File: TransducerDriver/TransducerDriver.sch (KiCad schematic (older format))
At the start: 18 parts, among them Q3 IRF540N, Q4 IRF540N, T2 Transformer_SP_1S 1:10

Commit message: studies on transducer
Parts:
- removed C?: 159nF, symbol Device:C
- removed C?: 10nF, symbol Device:C
- removed R? (x2): 4K, symbol Device:R
- removed R?: 2Khom, symbol Device:R
- removed R?: 1Kohm, symbol Device:R
- removed R? (x2): 101, symbol Device:R
- removed Rshut3: 0.01, Resistors_THT:R_Axial_DIN0207_L6.3mm_D2.5mm_P10.16mm_Horizontal, symbol Device:R
- removed Rtrans2: 10K, Resistors_THT:R_Axial_DIN0207_L6.3mm_D2.5mm_P10.16mm_Horizontal, symbol Device:R
- removed U? (x2): INA217, symbol Amplifier_Instrumentation:INA217
- added C2In1, C2In2, C2out1, C3, C4, Cgnd2, Cref2: 0.1u, Capacitors_THT:C_Disc_D5.0mm_W2.5mm_P5.00mm, symbol Device:C_Small
- added Cadc1: 10pf, Capacitors_THT:C_Disc_D8.0mm_W5.0mm_P7.50mm, symbol Device:C
- added Cb1: 10nF, Capacitors_THT:C_Disc_D5.0mm_W2.5mm_P5.00mm, symbol Device:C_Small
- added Cb?: 0.1uF, Capacitors_THT:C_Disc_D5.0mm_W2.5mm_P5.00mm, symbol Device:C_Small
- added Cenv1: 10nf, Capacitors_THT:C_Disc_D5.0mm_W2.5mm_P5.00mm, symbol Device:C_Small
- added Cg1: 0.47uF, Capacitors_THT:C_Disc_D5.0mm_W2.5mm_P5.00mm, symbol Device:C_Small
- added D2: 1N4007, Diodes_THT:D_DO-35_SOD27_P10.16mm_Horizontal, symbol Device:D
- added Dz1, Dz2, Dz3: 3.3V, symbol Device:D_Zener
- added J1: ModSigJack, symbol Connector:Conn_01x02_Female
- added J2: BattJack+, symbol Connector:Conn_01x01_Male
- added J3: BattJack-, symbol Connector:Conn_01x01_Male
- added Jadc1: connADC, symbol Connector:Conn_01x01_Male
- added R2: 1K, Resistors_THT:R_Axial_DIN0207_L6.3mm_D2.5mm_P10.16mm_Horizontal, symbol Device:R
- added R2F1: 100Kohm, Resistors_THT:R_Axial_DIN0309_L9.0mm_D3.2mm_P12.70mm_Horizontal, symbol Device:R
- added R2G1: 1Kohm, Resistors_THT:R_Axial_DIN0309_L9.0mm_D3.2mm_P12.70mm_Horizontal, symbol Device:R
- added Radc1: 2.5K, Resistors_THT:R_Axial_DIN0309_L9.0mm_D3.2mm_P12.70mm_Horizontal, symbol Device:R
- added Rb1, Rb2: 5K, Resistors_THT:R_Axial_DIN0309_L9.0mm_D3.2mm_P12.70mm_Horizontal, symbol Device:R
- added Rbias1, Rbias2: 2.2K, Resistors_THT:R_Axial_DIN0309_L9.0mm_D3.2mm_P12.70mm_Horizontal, symbol Device:R
- added Rbuf1: 10ohm, Resistors_THT:R_Axial_DIN0309_L9.0mm_D3.2mm_P12.70mm_Horizontal, symbol Device:R
- added Rf2, Rin2: 200K, Resistors_THT:R_Axial_DIN0309_L9.0mm_D3.2mm_P12.70mm_Horizontal, symbol Device:R
- added Rg1: 2K, Resistors_THT:R_Axial_DIN0309_L9.0mm_D3.2mm_P12.70mm_Horizontal, symbol Device:R
- added Rgain1: 101, Resistors_THT:R_Axial_DIN0309_L9.0mm_D3.2mm_P12.70mm_Horizontal, symbol Device:R
- added U1: TL082, symbol Amplifier_Operational:TL082
- added U2: INA217-Amplifier_Instrumentation, symbol TransducerDriver-rescue:INA217-Amplifier_Instrumentation
- added U3: TC427, Housings_DIP:DIP-8_W7.62mm_LongPads, symbol TransducerDriver-rescue:TC427-Driver_FET
- added U4: LM4562, symbol Amplifier_Operational:LM4562
- added Y2: Crystal, Wire_Connections_Bridges:WireConnection_2.50mmDrill, symbol Device:Crystal
- added Y3: FishFinder, Wire_Connections_Bridges:WireConnection_2.50mmDrill, symbol Device:Crystal
- D1: renamed from D?; footprint (none) -> Diodes_THT:D_5W_P12.70mm_Horizontal
- Q3, Q4: footprint Package_TO_SOT_THT:TO-220-3_Vertical -> TO_SOT_Packages_THT:TO-220-3_Vertical
- Renv1: renamed from R?; value 530 -> 2K; footprint (none) -> Resistors_THT:R_Axial_DIN0309_L9.0mm_D3.2mm_P12.70mm_Horizontal
- T1: renamed from T2; footprint Transformer_THT:Transformer_Toroid_Tapped_Horizontal_D10.5mm_Amidon-T37 -> Transformers_THT:Transformer_Toroid_Tapped_Horizontal_D14.0mm_Amidon-T50
- Y1: renamed from Y?; footprint (none) -> Wire_Connections_Bridges:WireConnection_2.50mmDrill
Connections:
- net labels added: ADCinput, ModSig+, ModSig-, Prob1, Prob2, Stage1Out, Stage2Out, Vin
- net labels removed: MicroInput, SigA, SigB, VCC
- wire segments 60 -> 125
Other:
- note added: "10Khz HP filter\n0.1uF 1Kohm"
- note added: "6Kohm Internal \nR. Is it High \noutput Impedance?"
- note added: "ADC internal"
- note added: "Envelope\nDetector"
- note added: "First Stage \nDiff Amp"
- note added: "Impedance Measure Circuit"
- note added: "Inverting \nSimple Vref"
- note added: "Measure"
- note added: "Non-Inverting\nHigh Impedance"
- note added: "Potential\nVariable \nGain"
- note added: "Rin2 same as R2 \nlimit input bias current"
- note added: "Transmitter"
- note added: "Two Options for second stage"
- note added: "Vref Gen"
- note added: "X cgnd1<<Rg2 \nF = 20Khz\nC = 0.47uF \nXc = 17ohm"
- note added: "bias current \nsupply\n0.1uF 2.2Kohm\nFc = 4.5Khz"
- note added: "half battery Vref generator \nwith small resistor Rbuf1\nprevernt opamp unstable"
- note added: "min Fcarr = 40Khz \nmax Fmod = 1Khz \n10nF 2Kohm\nFc = 8Kohm"
- note added: "sine wave input"
- note removed: "-3dB @ 30Khz"
- note removed: "40dB gain\n= 101ohm RG"
- note removed: "6K output impedence"
- note removed: "Driver"
- note removed: "Highpass Assuming \n1K impedance. \n1Khz cutoff feq"
- note removed: "Over Amplify \nthen voltage devide \nto reduce diode bias"
- note removed: "amplify signal at \nhalf battery voltage. \n(fake negative voltage)"
- moved on the sheet: D1, Q3, Renv1, T1, Y1

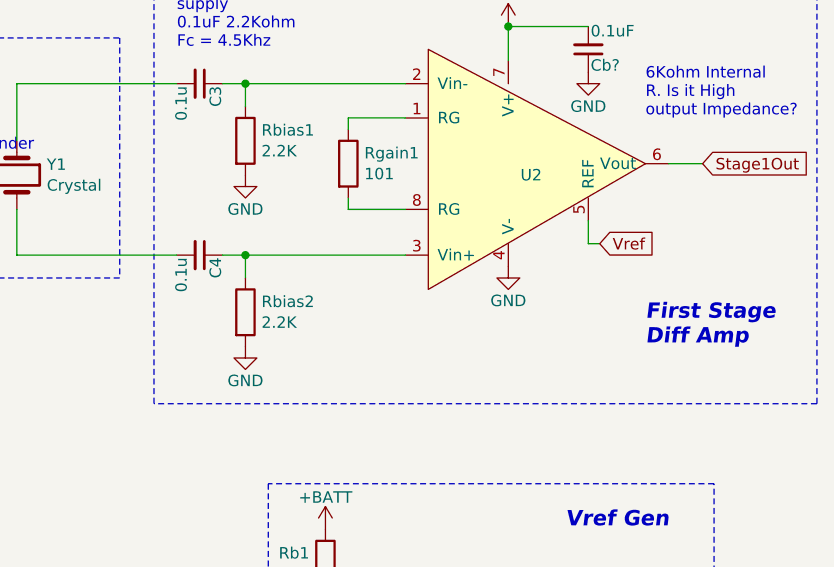
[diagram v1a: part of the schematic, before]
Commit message: small change on InsAmp. Input pull to vref
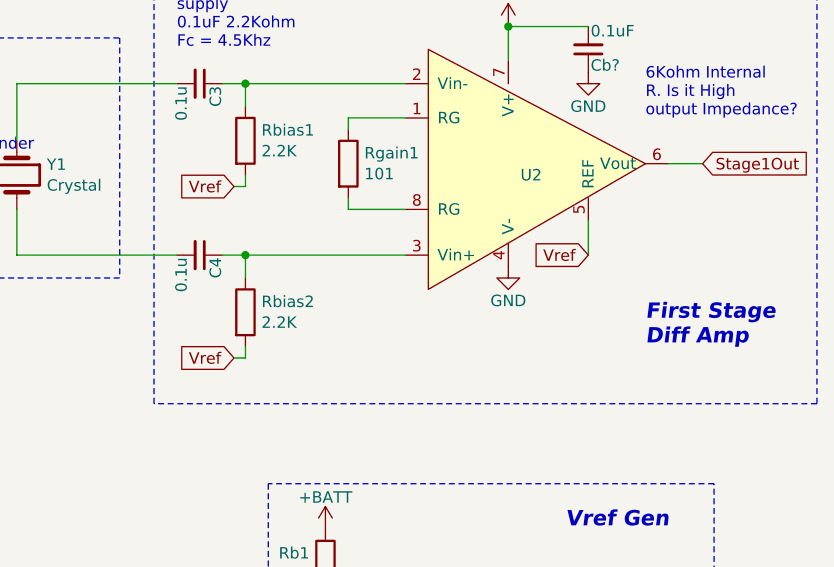
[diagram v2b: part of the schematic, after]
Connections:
- net GND: no longer Rbias1.2, Rbias2.2
- net Vref: now also Rbias1.2, Rbias2.2
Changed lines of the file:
@@
-	1    0    0    -1
-$EndComp
-$Comp
-L power:GND #PWR02
-U 1 1 5E45D892
-P 2050 4150
-F 0 "#PWR02" H 2050 3900 50  0001 C CNN
-F 1 "GND" H 2050 4000 50  0000 C CNN
-F 2 "" H 2050 4150 50  0001 C CNN
-F 3 "" H 2050 4150 50  0001 C CNN
-	1    2050 4150
-	1    0    0    -1
-$EndComp
-$Comp
-L power:GND #PWR03
-U 1 1 5E45D96F
-P 2050 4900
-F 0 "#PWR03" H 2050 4650 50  0001 C CNN
-F 1 "GND" H 2050 4750 50  0000 C CNN
-F 2 "" H 2050 4900 50  0001 C CNN
-F 3 "" H 2050 4900 50  0001 C CNN
-	1    2050 4900
 	1    0    0    -1
 $EndComp
@@
 	2750 4500 2050 4500
 Connection ~ 2050 4500
-Text GLabel 3600 4450 2    50   Input ~ 0
+Text GLabel 3550 4500 0    50   Input ~ 0
 Vref
-Wire Wire Line
-	3550 4350 3550 4450
-Wire Wire Line
-	3550 4450 3600 4450
 $Comp
 L Device:R Rbuf1
@@
 Wire Wire Line
 	6850 2050 7150 2050
+Text GLabel 2000 4200 0    50   Input ~ 0
+Vref
+Wire Wire Line
+	2050 4150 2050 4200
+Wire Wire Line
+	2050 4200 2000 4200
+Text GLabel 2000 4950 0    50   Input ~ 0
+Vref
+Wire Wire Line
+	2050 4900 2050 4950
+Wire Wire Line
+	2050 4950 2000 4950
+Wire Wire Line
+	3550 4350 3550 4500
 $EndSCHEMATC
